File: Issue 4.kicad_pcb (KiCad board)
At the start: 2 copper layers, 213.4 x 130.8 mm, 199 parts, among them IC1 ULA, IC10 4116, IC11 4116, IC12 4116, IC13 4116, IC14 LM1889, IC15 4532, IC16 4532, IC17 4532, IC18 4532, IC19 4532, IC2 Z80, IC20 4532, IC21 4532, IC22 4532, IC23 74LS32, IC24 74LS00, IC25 74LS157, IC26 74LS157, IC3 LS157, IC4 LS157, IC5 ROM, IC6 4116, IC7 4116, IC8 4116, IC9 4116, J1 OKI, J10 UR3, J11 UR4, J2 TI, J3 TI, J4 TI, J7 Barrel_Jack_MountingPin, J8 UR1, J9 UR2, T1 Coil, X1 14Mhz, X2 4.43Mhz

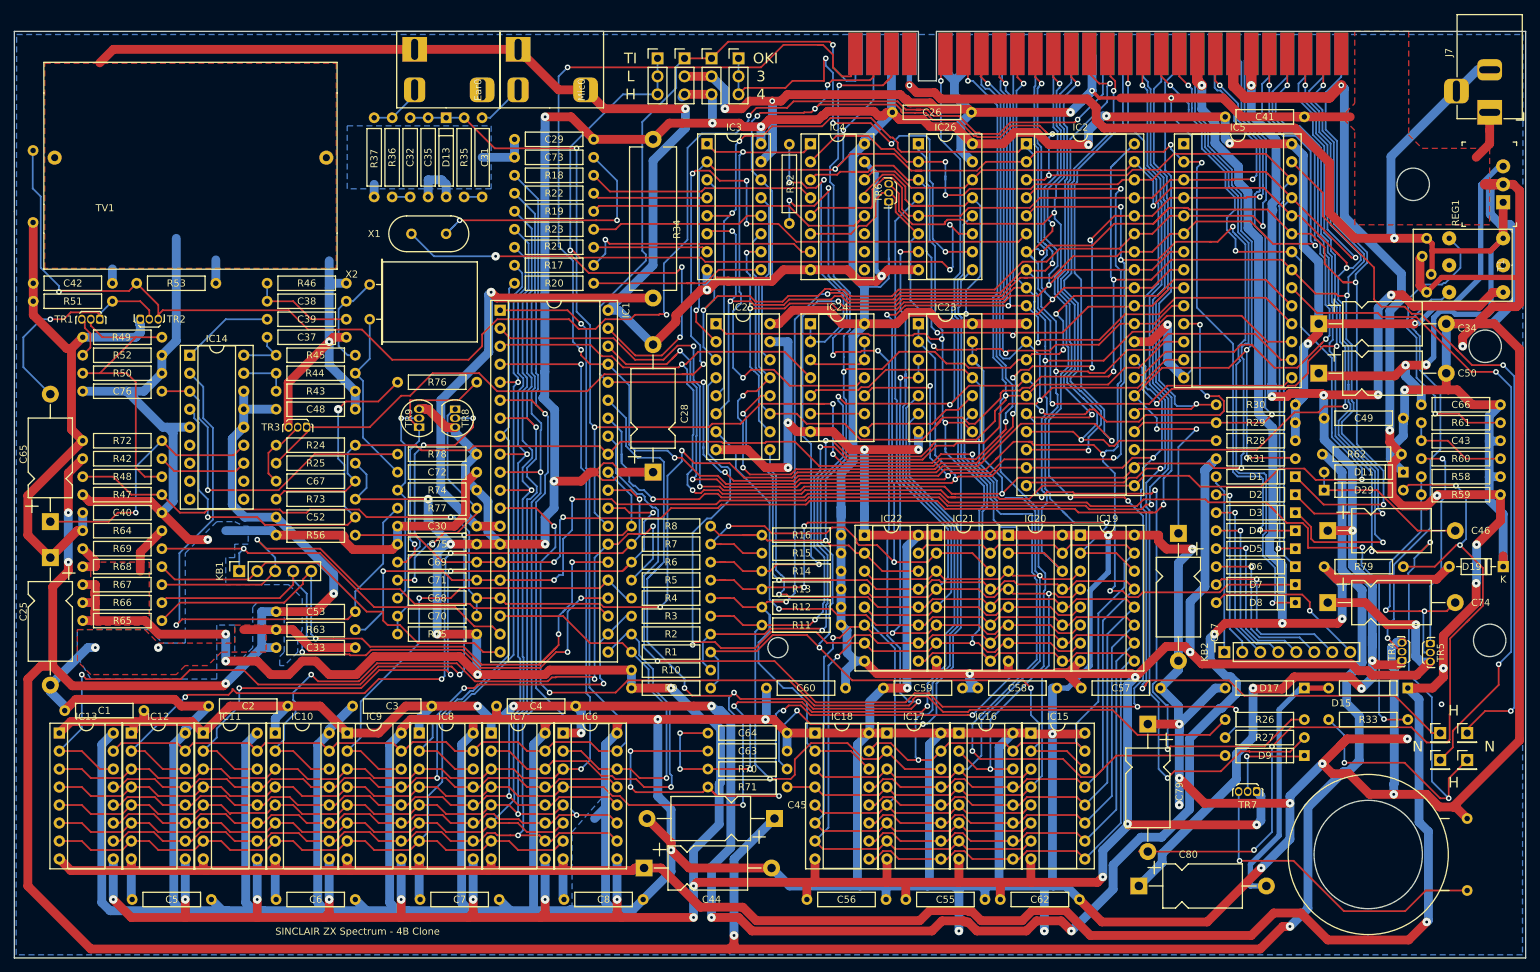
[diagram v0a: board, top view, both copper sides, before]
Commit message: Updated to recent Kicad
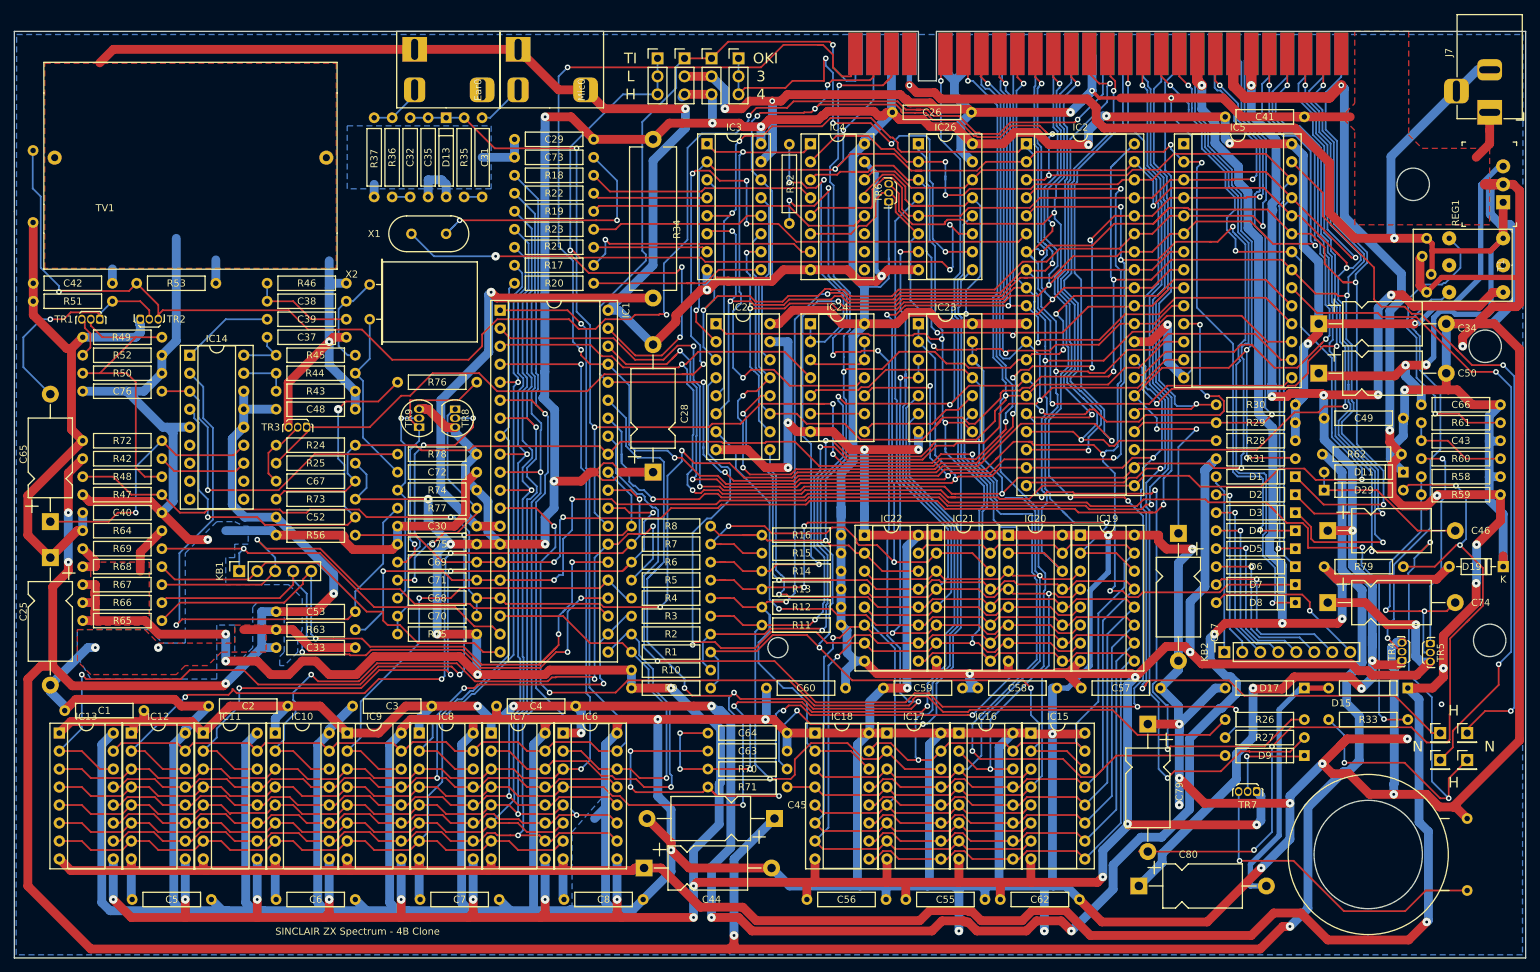
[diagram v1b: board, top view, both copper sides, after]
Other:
- net class Default removed
- net class PArtial removed
- net class Power removed
